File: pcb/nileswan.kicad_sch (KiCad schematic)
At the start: 8 parts, among them J1 Micro_SD_Card_Det_Hirose_DM3AT

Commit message: second pcb iteration
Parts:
- added C11, C13, C24, C25: 1 μF, Capacitor_SMD:C_0603_1608Metric, symbol Device:C
- added C27: 470 pF, Capacitor_SMD:C_0402_1005Metric, symbol Device:C
- added C28: 4.7 nF, Capacitor_SMD:C_0402_1005Metric, symbol Device:C
- added C29, C30, C5: 100 nF, Capacitor_SMD:C_0402_1005Metric, symbol Device:C
- added J3: SM02B-SRSS-TB_LF__SN_, snapeda:SM02B-SRSS-TB_LF__SN_, symbol SM02B-SRSS-TB:SM02B-SRSS-TB_LF__SN_
- added J4: Conn_02x05_Counter_Clockwise, Connector:Tag-Connect_TC2050-IDC-NL_2x05_P1.27mm_Vertical, symbol Connector_Generic:Conn_02x05_Counter_Clockwise
- added R18: 118k, Resistor_SMD:R_0402_1005Metric, symbol Device:R
- added R19: 75k, Resistor_SMD:R_0402_1005Metric, symbol Device:R
- added R3: 47k, Resistor_SMD:R_0402_1005Metric, symbol Device:R
- added R4, R6, R7: 10k, Resistor_SMD:R_0402_1005Metric, symbol Device:R
- added U2: W25Q16JVUXIQ, snapeda:SON50P300X200X60-9N, symbol nileswan:W25Q16JVUXIQ
- added U3: AP2127N-1.2, Package_TO_SOT_SMD:SOT-23, symbol Regulator_Linear:AP2127N-1.2
- added U5: AP22966DC8-7, snapeda:IC_AP22966DC8-7, symbol AP22966DC8-7:AP22966DC8-7
- added U7: TPS3613, Package_SO:VSSOP-10_3x3mm_P0.5mm, symbol nileswan:TPS3613
- R10, R2, R9: footprint Resistor_SMD:R_0603_1608Metric -> Resistor_SMD:R_0402_1005Metric
- R5: value 47k -> 10k; footprint Resistor_SMD:R_0603_1608Metric -> Resistor_SMD:R_0402_1005Metric
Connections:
- net fpga/SD_DAT0 is gone; now on net fpga/TF_POCI: J1.7 (DAT0)
- net 3.3V: now also C11.1, C29.1, C5.1, J4.1 (Pin_1), R18.1, R4.1, R6.1, U2.8 (VCC), U3.3 (VI), U5.13_14 (VOUT1), U7.2 (Vdd); no longer C1.1, J1.4 (VDD), R1.1, R10.1, R9.1
- net GND: now also C11.2, C13.2, C24.2, C25.2, C27.2, C28.2, C29.2, C30.2, C5.2, J3.1, J4.2 (Pin_2), R19.2, U2.4 (GND), U2.9 (EP), U3.1 (GND), U5.11 (GND), U5.15 (EXP), U7.3 (GND)
- net at J1.8 (DAT1): now also R3.2; no longer R5.2
- net fpga/TF_POCI: now reaches R9.2
- net fpga/TF_POCI: no longer J1.2 (DAT3/CD)
- net fpga/SD_CLK renamed fpga/TF_CLK
- net fpga/SD_CMD renamed fpga/TF_PICO
- net fpga/SD_DETECT renamed fpga/TF_DETECT
- new net: J3.2, U7.10 (Vbat)
- new net: R18.2, R19.1, U7.8 (SENSE)
- new net: C24.1, C25.1, R1.1, R7.1, U5.1_2 (VIN1), U5.4 (VBIAS), U5.6_7 (VIN2)
- new net: C28.1, U5.10 (SS2)
- new net: C27.1, U5.12 (SS1)
- new net: R7.2, U5.3 (EN1)
- new net: R5.2, U2.3 (/WP)
- new net: R6.2, U2.7 (IO3)
- new net 1.2V: C13.1, U3.2 (VO)
- new net 3.3V_SRAM: C30.1, U7.1 (Vout)
- new net 3.3V_TF: C1.1, J1.4 (VDD), R10.1, R3.1, R9.1, U5.8_9 (VOUT2)
- new net fpga/CRESET_B: J4.6 (Pin_6)
- new net fpga/FLASH_CLK: J4.9 (Pin_9), U2.6 (CLK)
- new net fpga/FLASH_CS: J4.10 (Pin_10), R4.2, U2.1 (/CS)
- new net fpga/FLASH_PICO: J4.7 (Pin_7), U2.2 (DO)
- new net fpga/FLASH_POCI: J4.8 (Pin_8), U2.5 (DI)
- new net fpga/TF_POW: U5.5 (EN2)
- new net fpga/TF_SEL: J1.2 (DAT3/CD)
- new net fpga//SEL_SRAM: U7.5 (/CEIN)
- new net memory//SEL_SRAM: U7.6 (/CEOUT)
- no-connect marks 2 -> 8
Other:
- sheet fpga ports: added CRESET_B, FLASH_CLK, FLASH_CS, FLASH_PICO, FLASH_POCI, TF_CLK, TF_DETECT, TF_PICO, TF_POCI, TF_POW, TF_SEL, /PSRAM_LB, /PSRAM_UB, /SEL_SRAM; removed ENABLE_OUT_PSRAM, SD_CLK, SD_CMD, SD_DAT0, SD_DETECT
- sheet memory ports: added A_HIGH[0..6], /PSRAM_LB, /PSRAM_UB, /SEL_SRAM; removed A_HIGH[0..5], ENABLE_OUT_PSRAM
- note added: "For the calculation of the sense resistors see: https://www.ti.com/lit/an/slva450b/slva450b.pdf?ts=1706371120130 Resistor values were as in the example, except for Vref = 1.15 V"
- moved on the sheet: C1, J1, R10, R2, R9

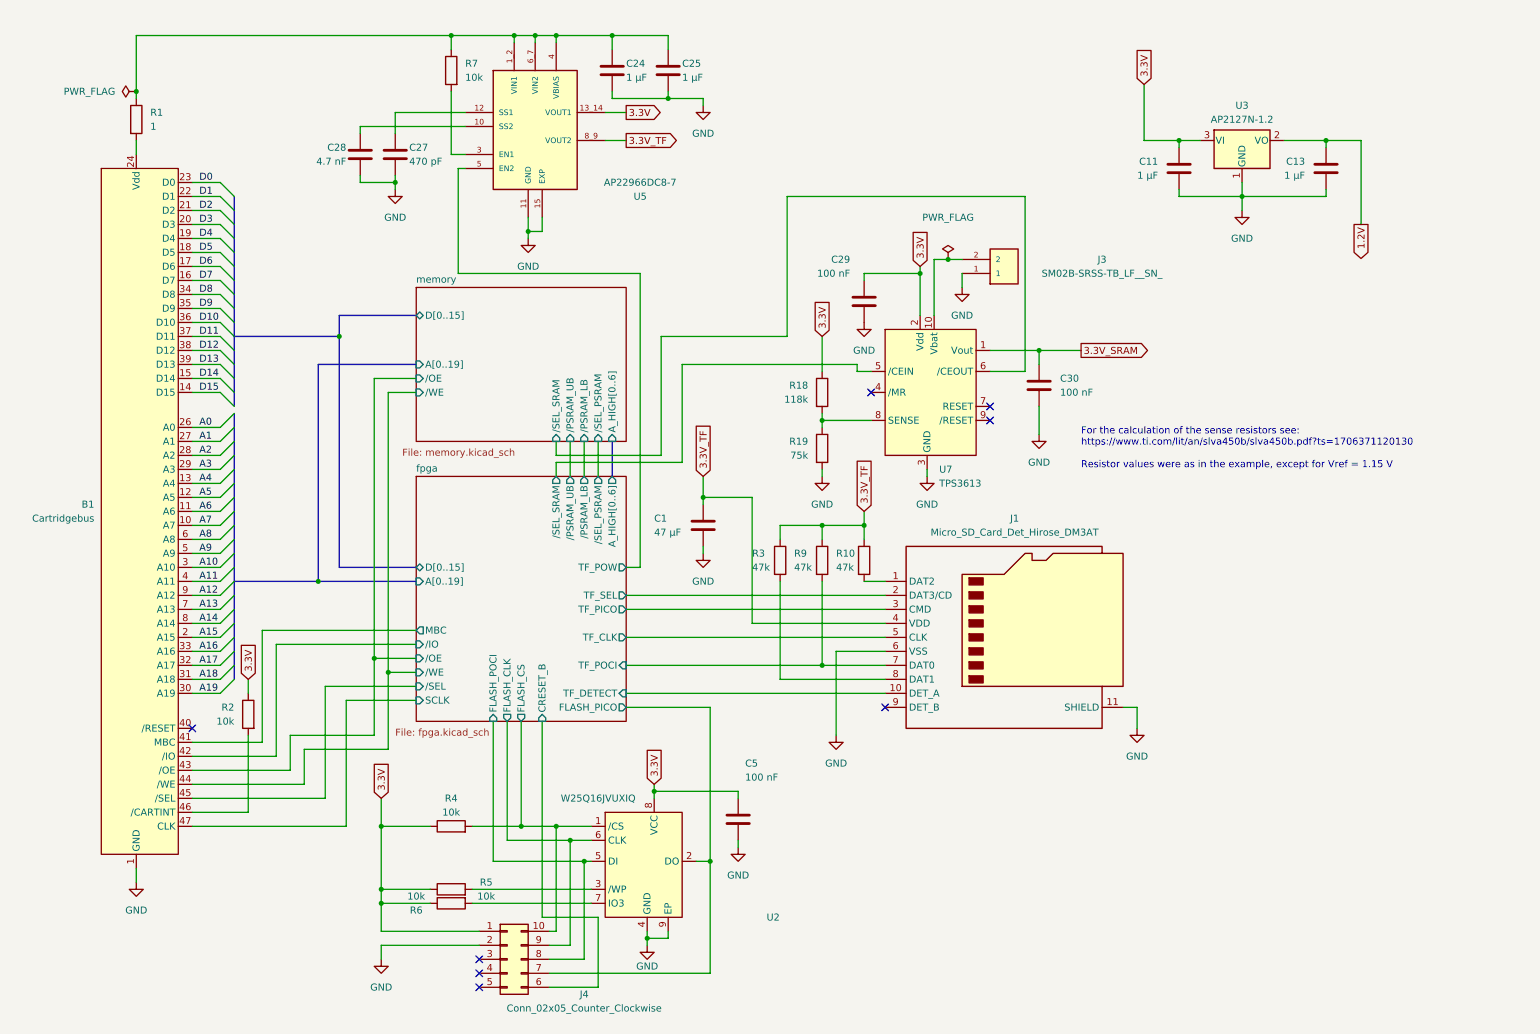
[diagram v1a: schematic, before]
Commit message: pcb revision 3 and 16 MB PSRAM support
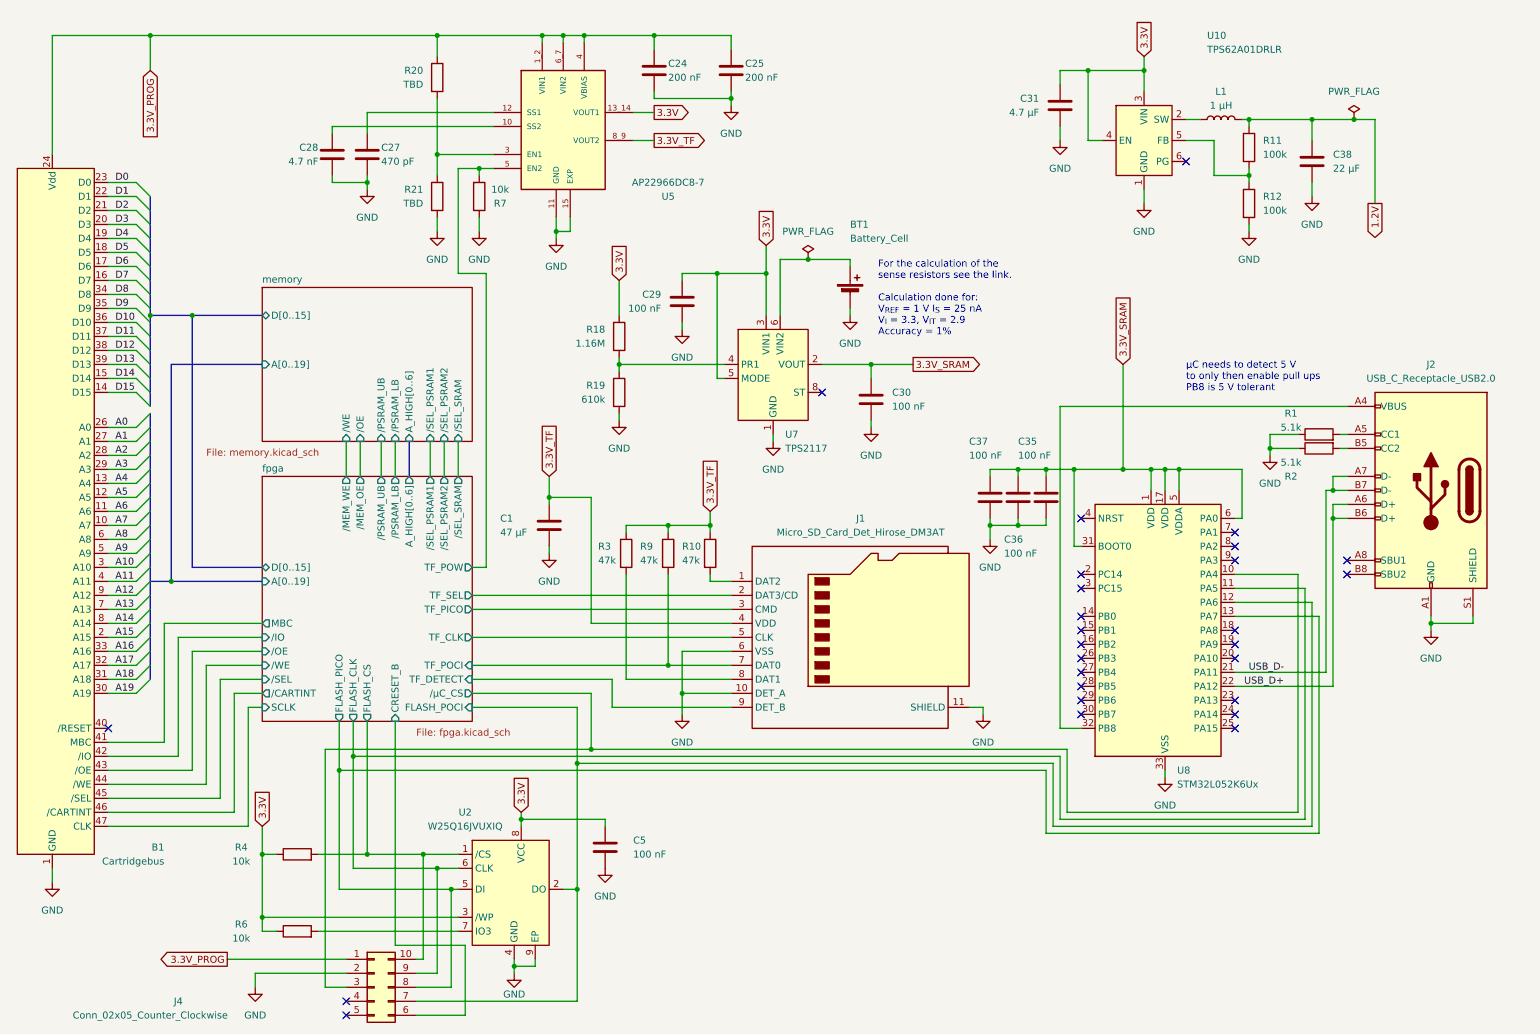
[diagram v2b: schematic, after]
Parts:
- removed C11, C13: 1 μF, Capacitor_SMD:C_0603_1608Metric, symbol Device:C
- removed J3: SM02B-SRSS-TB_LF__SN_, snapeda:SM02B-SRSS-TB_LF__SN_, symbol SM02B-SRSS-TB:SM02B-SRSS-TB_LF__SN_
- removed R5: 10k, Resistor_SMD:R_0402_1005Metric, symbol Device:R
- removed U3: AP2127N-1.2, Package_TO_SOT_SMD:SOT-23, symbol Regulator_Linear:AP2127N-1.2
- removed U7: TPS3613, Package_SO:VSSOP-10_3x3mm_P0.5mm, symbol nileswan:TPS3613
- added BT1: Battery_Cell, snapeda:BAT_BAT-HLD-012-SMT, symbol Device:Battery_Cell
- added C31: 4.7 μF, Capacitor_SMD:C_0603_1608Metric, symbol Device:C
- added C35, C36, C37: 100 nF, Capacitor_SMD:C_0402_1005Metric, symbol Device:C
- added C38: 22 μF, Capacitor_SMD:C_0603_1608Metric, symbol Device:C
- added J2: USB_C_Receptacle_USB2.0, Connector_USB:USB_C_Receptacle_GCT_USB4110, symbol Connector:USB_C_Receptacle_USB2.0
- added L1: 1 μH, Inductor_SMD:L_Murata_DFE201610P, symbol Device:L
- added R11: 100k, Resistor_SMD:R_0402_1005Metric, symbol Device:R
- added R12: 100k, Capacitor_SMD:C_0402_1005Metric, symbol Device:R
- added R20, R21: TBD, Resistor_SMD:R_0402_1005Metric, symbol Device:R
- added U10: TPS62A01DRLR, Package_TO_SOT_SMD:SOT-563, symbol nileswan:TPS62A01DRLR
- added U7: TPS2117, snapeda:SOTFL50P160X60-8N, symbol nileswan:TPS2117
- added U8: STM32L052K6Ux, Package_DFN_QFN:QFN-32-1EP_5x5mm_P0.5mm_EP3.45x3.45mm, symbol MCU_ST_STM32L0:STM32L052K6Ux
- C24, C25: value 1 μF -> 200 nF; footprint Capacitor_SMD:C_0603_1608Metric -> Capacitor_SMD:C_0402_1005Metric
- R1: value 1 -> 5.1k; footprint Resistor_SMD:R_0603_1608Metric -> Resistor_SMD:R_0402_1005Metric
- R18: value 118k -> 1.16M
- R19: value 75k -> 610k
- R2: value 10k -> 5.1k
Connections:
- net 1.2V: now also C38.1, L1.2, R11.1
- net 3.3V: now also U2.3 (/WP), C31.1, U10.3 (VIN), U10.4 (EN), U7.3 (VIN1), U7.5 (MODE); no longer J4.1 (Pin_1), R2.1
- net 3.3V_SRAM: now also C35.1, C36.1, C37.1, U7.2 (VOUT), U7.7 (VOUT), U8.1 (VDD), U8.17 (VDD), U8.31 (BOOT0), U8.5 (VDDA), U8.6 (PA0)
- net GND: now also J1.10 (DET_A), R1.1, R2.1, R7.1, BT1.2 (-), C31.2, C35.2, C36.2, C37.2, C38.2, J2.A1 (GND), J2.A12 (GND), J2.B1 (GND), J2.B12 (GND), J2.S1 (SHIELD), R12.2, R21.2, U10.1 (GND), U7.1 (GND), U8.33 (VSS)
- net fpga/FLASH_CLK: now also U8.11 (PA5)
- net fpga/FLASH_PICO: now also J4.8 (Pin_8), U2.5 (DI), U8.13 (PA7); no longer J4.7 (Pin_7), U2.2 (DO)
- net fpga/FLASH_POCI: now also J4.7 (Pin_7), U2.2 (DO), U8.12 (PA6); no longer J4.8 (Pin_8), U2.5 (DI)
- net fpga/TF_DETECT: now also J1.9 (DET_B); no longer J1.10 (DET_A)
- net fpga/TF_POW: now also R7.2
- net at R18.2, R19.1: now also U7.4 (PR1)
- net 3.3V_PROG: now reaches C24.1, C25.1, U5.1_2 (VIN1), U5.4 (VBIAS), U5.6_7 (VIN2)
- net 3.3V_PROG: now also B1.24 (Vdd), B1.25 (Vdd), J4.1 (Pin_1), R20.1; no longer R1.1, R7.1
- net fpga//μC_CS: now reaches J4.3 (Pin_3)
- net fpga//μC_CS: now also U8.10 (PA4)
- net at U5.3 (EN1): now also R20.2, R21.1; no longer R7.2
- net at R2.2: now also J2.B5 (CC2); no longer B1.46 (/CARTINT)
- new net: BT1.1 (+), U7.6 (VIN2)
- new net: J2.A4 (VBUS), J2.A9 (VBUS), J2.B4 (VBUS), J2.B9 (VBUS), U8.32 (PB8)
- new net: J2.A5 (CC1), R1.2
- new net: L1.1, U10.2 (SW)
- new net: R11.2, R12.1, U10.5 (FB)
- new net USB_D+: J2.A6 (D+), J2.B6 (D+), U8.22 (PA12)
- new net USB_D-: J2.A7 (D-), J2.B7 (D-), U8.21 (PA11)
- new net fpga//CARTINT: B1.46 (/CARTINT)
- no-connect marks 8 -> 27
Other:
- sheet fpga ports: added /CARTINT, /MEM_OE, /MEM_WE, /SEL_PSRAM1, /SEL_PSRAM2, /μC_CS; removed /SEL_PSRAM
- sheet memory ports: added /SEL_PSRAM1, /SEL_PSRAM2; removed /SEL_PSRAM
- note added: "For the calculation of the sense resistors see the link. Calculation done for: V_{REF} = 1 V I_{S} = 25 nA V_{I} = 3.3, V_{IT} = 2.9 Accuracy = 1%"
- note added: "μC needs to detect 5 V to only then enable pull ups PB8 is 5 V tolerant"
- note removed: "For the calculation of the sense resistors see: https://www.ti.com/lit/an/slva450b/slva450b.pdf?ts=1706371120130 Resistor values were as in the example, except for Vref = 1.15 V"
- moved on the sheet: B1, C1, C24, C25, C27, C28, C29, C30, C5, J1, J4, R10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

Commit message: use correct footprint for R12
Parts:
- R12: footprint Capacitor_SMD:C_0402_1005Metric -> Resistor_SMD:R_0402_1005Metric
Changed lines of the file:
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@@
       (effects (font (size 1.27 1.27)) (justify left))
     )
-    (property "Footprint" "Capacitor_SMD:C_0402_1005Metric" (at 236.982 48.26 90)
+    (property "Footprint" "Resistor_SMD:R_0402_1005Metric" (at 236.982 48.26 90)
       (effects (font (size 1.27 1.27)) hide)
     )
